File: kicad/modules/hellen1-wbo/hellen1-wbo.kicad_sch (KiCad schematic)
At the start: 58 parts, among them J600 Conn_02x03_Odd_Even, M600 Module-wbo-0.2, Q600 BTS3028, U600 MCP6004, U601 AD8628, U602 STM32F042K6Tx, U603 REF3033, U604 XC6206P332MR

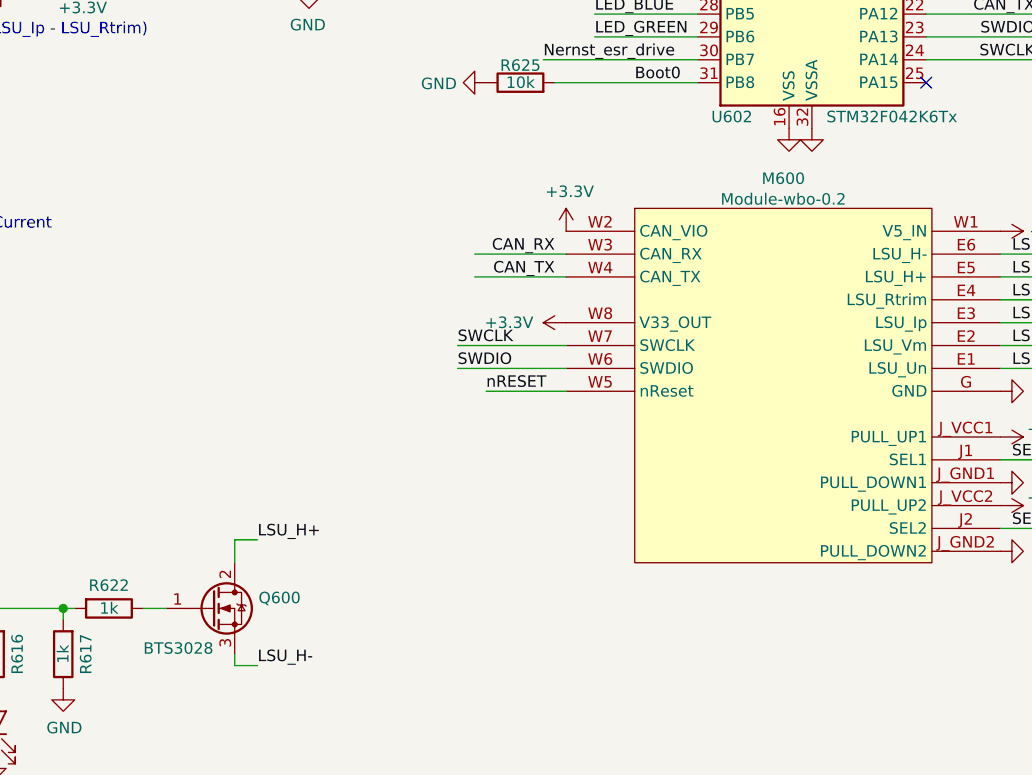
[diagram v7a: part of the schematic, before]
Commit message: wbo-0.3 https://github.com/andreika-git/hellen-one/issues/96
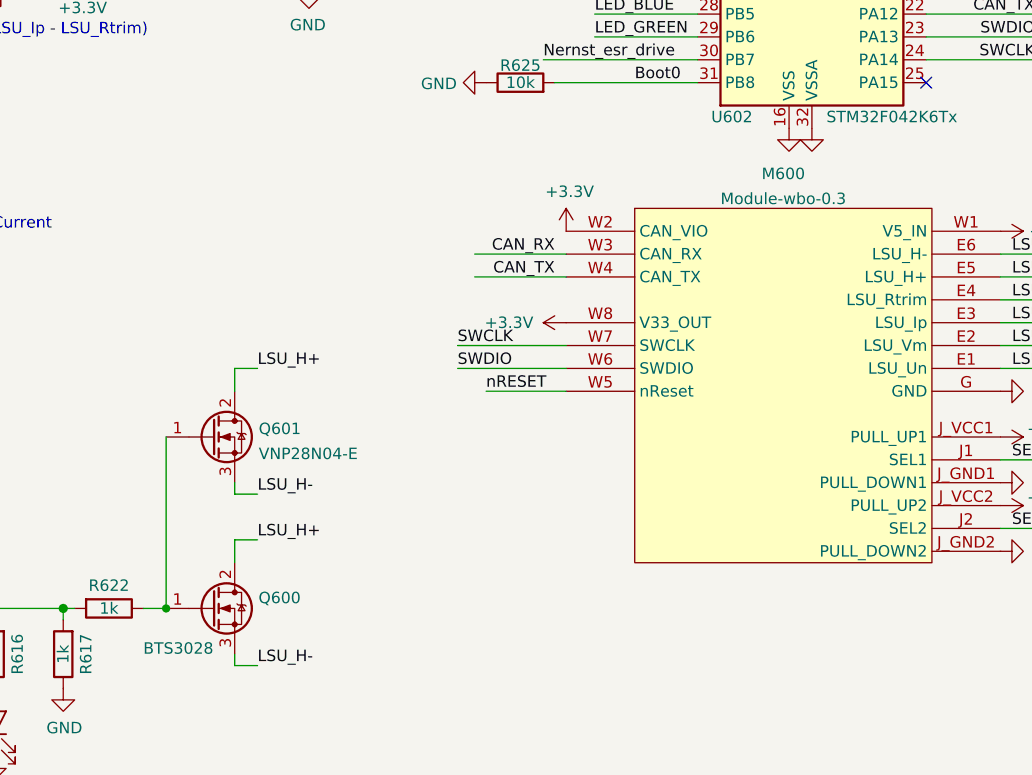
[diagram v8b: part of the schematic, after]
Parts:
- removed M600: Module-wbo-0.2, hellen-one-wbo-0.2:wbo, symbol hellen-one-wbo-0.2:Module-wbo-0.2
- added M600: Module-wbo-0.3, hellen-one-wbo-0.3:wbo, symbol hellen-one-wbo-0.3:Module-wbo-0.3
- added Q601: VNP28N04-E, Package_TO_SOT_THT:TO-220-3_Vertical, symbol Transistor_FET:VNP10N07
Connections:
- net +3V3: now also M600.J_VCC1 (PULL_UP1), M600.J_VCC2 (PULL_UP2), M600.W2 (CAN_VIO), M600.W8 (V33_OUT)
- net +5V: now also M600.W1 (V5_IN)
- net CAN_RX: now also M600.W3 (CAN_RX)
- net CAN_TX: now also M600.W4 (CAN_TX)
- net GND: now also M600.G (GND), M600.J_GND1 (PULL_DOWN1), M600.J_GND2 (PULL_DOWN2)
- net LSU_H+: now also M600.E5 (LSU_H+), Q601.2 (D)
- net LSU_H-: now also M600.E6 (LSU_H-), Q601.3 (S)
- net LSU_Ip: now also M600.E3 (LSU_Ip)
- net LSU_Rtrim: now also M600.E4 (LSU_Rtrim)
- net LSU_Un: now also M600.E1 (LSU_Un)
- net LSU_Vm: now also M600.E2 (LSU_Vm)
- net SEL1: now also M600.J1 (SEL1)
- net SEL2: now also M600.J2 (SEL2)
- net SWCLK: now also M600.W7 (SWCLK)
- net SWDIO: now also M600.W6 (SWDIO)
- net nRESET: now also M600.W5 (nReset)
- net at Q600.1 (G), R622.1: now also Q601.1 (G)
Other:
- company: (none) -> rusefi.com
- title: (none) -> WBO
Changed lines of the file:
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@@
-(kicad_sch (version 20210406) (generator eeschema)
+(kicad_sch (version 20210621) (generator eeschema)
   (paper "A4")
+  (title_block
+    (title "WBO")
+    (date "2021-09-28")
+    (rev "0.3")
+    (company "rusefi.com")
+  )
   (junction (at 27.94 32.385) (diameter 1.016) (color 0 0 0 0))
   (junction (at 39.37 142.24) (diameter 1.016) (color 0 0 0 0))
@@
   (junction (at 115.57 27.94) (diameter 1.016) (color 0 0 0 0))
   (junction (at 115.57 33.02) (diameter 1.016) (color 0 0 0 0))
+  (junction (at 116.84 166.37) (diameter 0) (color 0 0 0 0))
   (junction (at 120.65 87.63) (diameter 1.016) (color 0 0 0 0))
   (junction (at 135.89 30.48) (diameter 1.016) (color 0 0 0 0))
@@
     (stroke (width 0) (type solid) (color 0 0 0 0))
   )
+  (wire (pts (xy 116.84 147.32) (xy 116.84 166.37))
+    (stroke (width 0) (type default) (color 0 0 0 0))
+  )
   (wire (pts (xy 116.84 166.37) (xy 114.3 166.37))
     (stroke (width 0) (type solid) (color 0 0 0 0))
@@
   )
   (wire (pts (xy 120.65 87.63) (xy 123.19 87.63))
+    (stroke (width 0) (type solid) (color 0 0 0 0))
+  )
+  (wire (pts (xy 124.46 139.7) (xy 127 139.7))
+    (stroke (width 0) (type solid) (color 0 0 0 0))
+  )
+  (wire (pts (xy 124.46 142.24) (xy 124.46 139.7))
+    (stroke (width 0) (type solid) (color 0 0 0 0))
+  )
+  (wire (pts (xy 124.46 152.4) (xy 124.46 153.67))
+    (stroke (width 0) (type solid) (color 0 0 0 0))
+  )
+  (wire (pts (xy 124.46 153.67) (xy 127 153.67))
     (stroke (width 0) (type solid) (color 0 0 0 0))
   )
@@
     (effects (font (size 1.27 1.27)) (justify right bottom))
   )
+  (label "LSU_H+" (at 127 139.7 0)
+    (effects (font (size 1.27 1.27)) (justify left bottom))
+  )
+  (label "LSU_H-" (at 127 153.67 0)
+    (effects (font (size 1.27 1.27)) (justify left bottom))
+  )
   (label "LSU_H+" (at 127 158.75 0)
     (effects (font (size 1.27 1.27)) (justify left bottom))
@@
   (symbol (lib_id "hellen1-wbo-rescue:+3.3V-power") (at 161.29 124.46 0) (unit 1)
     (in_bom yes) (on_board yes)
-    (property "Reference" "#PWR?" (id 0) (at 161.29 128.27 0)
+    (property "Reference" "#PWR01" (id 0) (at 161.29 128.27 0)
       (effects (font (size 1.27 1.27)) hide)
     )
@@
   (symbol (lib_id "hellen1-wbo-rescue:+3.3V-power") (at 161.29 134.62 90) (mirror x) (unit 1)
     (in_bom yes) (on_board yes)
-    (property "Reference" "#PWR?" (id 0) (at 165.1 134.62 0)
+    (property "Reference" "#PWR02" (id 0) (at 165.1 134.62 0)
       (effects (font (size 1.27 1.27)) hide)
     )
@@
   (symbol (lib_id "hellen1-wbo-rescue:+3.3V-power") (at 209.55 147.32 270) (unit 1)
     (in_bom yes) (on_board yes)
-    (property "Reference" "#PWR?" (id 0) (at 205.74 147.32 0)
+    (property "Reference" "#PWR03" (id 0) (at 205.74 147.32 0)
       (effects (font (size 1.27 1.27)) hide)
     )
@@
   (symbol (lib_id "hellen1-wbo-rescue:+3.3V-power") (at 209.55 154.94 270) (unit 1)
     (in_bom yes) (on_board yes)
-    (property "Reference" "#PWR?" (id 0) (at 205.74 154.94 0)
+    (property "Reference" "#PWR05" (id 0) (at 205.74 154.94 0)
       (effects (font (size 1.27 1.27)) hide)
     )
@@
   (symbol (lib_id "hellen1-wbo-rescue:GND-power") (at 209.55 152.4 90) (unit 1)
     (in_bom yes) (on_board yes)
-    (property "Reference" "#PWR?" (id 0) (at 215.9 152.4 0)
+    (property "Reference" "#PWR04" (id 0) (at 215.9 152.4 0)
       (effects (font (size 1.27 1.27)) hide)
     )
@@
   (symbol (lib_id "hellen1-wbo-rescue:GND-power") (at 209.55 160.02 90) (unit 1)
     (in_bom yes) (on_board yes)
-    (property "Reference" "#PWR?" (id 0) (at 215.9 160.02 0)
+    (property "Reference" "#PWR06" (id 0) (at 215.9 160.02 0)
       (effects (font (size 1.27 1.27)) hide)
     )
@@
     (pin "1")
     (pin "2")
+  )
+  (symbol (lib_id "Transistor_FET:VNP10N07") (at 121.92 147.32 0) (unit 1)
+    (in_bom yes) (on_board yes) (fields_autoplaced)
+    (property "Reference" "Q601" (id 0) (at 127.1271 146.4115 0)
+      (effects (font (size 1.27 1.27)) (justify left))
+    )
+    (property "Value" "VNP28N04-E" (id 1) (at 127.1271 149.1866 0)
+      (effects (font (size 1.27 1.27)) (justify left))
+    )
+    (property "Footprint" "Package_TO_SOT_THT:TO-220-3_Vertical" (id 2) (at 128.27 149.225 0)
+      (effects (font (size 1.27 1.27) italic) (justify left) hide)
+    )
+    (property "Datasheet" "" (id 3) (at 121.92 147.32 0)
+      (effects (font (size 1.27 1.27)) (justify left) hide)
+    )
+    (property "LCSC" "C263002" (id 4) (at 121.92 147.32 0)
+      (effects (font (size 1.27 1.27)) hide)
+    )
+    (pin "1")
+    (pin "2")
+    (pin "3")
+  )
+  (symbol (lib_id "hellen1-wbo-rescue:Q_NMOS_GDS-Device") (at 121.92 166.37 0) (unit 1)
+    (in_bom yes) (on_board yes)
+    (property "Reference" "Q600" (id 0) (at 127.1016 165.2016 0)
+      (effects (font (size 1.27 1.27)) (justify left))
+    )
+    (property "Value" "BTS3028" (id 1) (at 114.3 170.815 0)
+      (effects (font (size 1.27 1.27)) (justify left))
+    )
+    (property "Footprint" "Package_TO_SOT_SMD:TO-252-2" (id 2) (at 127 163.83 0)
+      (effects (font (size 1.27 1.27)) hide)
+    )
+    (property "Datasheet" "~" (id 3) (at 121.92 166.37 0)
+      (effects (font (size 1.27 1.27)) hide)
+    )
+    (property "LCSC" "C112639" (id 4) (at 121.92 166.37 0)
+      (effects (font (size 1.27 1.27)) hide)
+    )
+    (pin "1")
+    (pin "2")
+    (pin "3")
   )
   (symbol (lib_id "Connector_Generic:Conn_02x03_Odd_Even") (at 254 33.02 0) (unit 1)
@@
     (pin "5")
     (pin "6")
-  )
-  (symbol (lib_id "hellen1-wbo-rescue:Q_NMOS_GDS-Device") (at 121.92 166.37 0) (unit 1)
-    (in_bom yes) (on_board yes)
-    (property "Reference" "Q600" (id 0) (at 127.1016 165.2016 0)
-      (effects (font (size 1.27 1.27)) (justify left))
-    )
-    (property "Value" "BTS3028" (id 1) (at 114.3 170.815 0)
-      (effects (font (size 1.27 1.27)) (justify left))
-    )
-    (property "Footprint" "Package_TO_SOT_SMD:TO-252-2" (id 2) (at 127 163.83 0)
-      (effects (font (size 1.27 1.27)) hide)
-    )
-    (property "Datasheet" "~" (id 3) (at 121.92 166.37 0)
-      (effects (font (size 1.27 1.27)) hide)
-    )
-    (property "LCSC" "C112639" (id 4) (at 121.92 166.37 0)
-      (effects (font (size 1.27 1.27)) hide)
-    )
-    (pin "1")
-    (pin "2")
-    (pin "3")
   )
   (symbol (lib_id "hellen1-wbo-rescue:XC6206PxxxMR-Regulator_Linear") (at 250.825 139.065 0) (unit 1)
@@
     (pin "9")
   )
-  (symbol (lib_id "hellen-one-wbo-0.2:Module-wbo-0.2") (at 168.91 121.92 0) (unit 1)
+  (symbol (lib_id "hellen-one-wbo-0.3:Module-wbo-0.3") (at 168.91 121.92 0) (unit 1)
     (in_bom yes) (on_board yes) (fields_autoplaced)
-    (property "Reference" "M600" (id 0) (at 185.42 118.6138 0))
-    (property "Value" "Module-wbo-0.2" (id 1) (at 185.42 120.9125 0))
-    (property "Footprint" "hellen-one-wbo-0.2:wbo" (id 2) (at 194.31 120.65 0)
+    (property "Reference" "M600" (id 0) (at 185.42 118.0804 0))
+    (property "Value" "Module-wbo-0.3" (id 1) (at 185.42 120.8555 0))
+    (property "Footprint" "hellen-one-wbo-0.3:wbo" (id 2) (at 194.31 120.65 0)
       (effects (font (size 1.27 1.27)) hide)
     )
@@
       (reference "#FLG0601") (unit 1) (value "PWR_FLAG") (footprint "")
     )
+    (path "/85464752-66ec-4a65-8d45-ea14c184e4d2"
+      (reference "#PWR01") (unit 1) (value "+3.3V") (footprint "")
+    )
+    (path "/6ac4b304-1d58-401a-a4a8-775f6dbed43e"
+      (reference "#PWR02") (unit 1) (value "+3.3V") (footprint "")
+    )
+    (path "/ff6c7081-9e18-4197-bee7-9f242433e34c"
+      (reference "#PWR03") (unit 1) (value "+3.3V") (footprint "")
+    )
+    (path "/60473116-363f-4ad0-a211-e8668ba00e3f"
+      (reference "#PWR04") (unit 1) (value "GND") (footprint "")
+    )
+    (path "/f3278198-5958-4dd8-bc33-4373cfed78c1"
+      (reference "#PWR05") (unit 1) (value "+3.3V") (footprint "")
+    )
+    (path "/b74a179f-999b-42b0-958b-4fe7f057860c"
+      (reference "#PWR06") (unit 1) (value "GND") (footprint "")
+    )
     (path "/00000000-0000-0000-0000-00005eb130b2"
       (reference "#PWR0600") (unit 1) (value "GND") (footprint "")
@@
       (reference "#PWR0649") (unit 1) (value "GND") (footprint "")
     )
-    (path "/60473116-363f-4ad0-a211-e8668ba00e3f"
-      (reference "#PWR?") (unit 1) (value "GND") (footprint "")
-    )
-    (path "/6ac4b304-1d58-401a-a4a8-775f6dbed43e"
-      (reference "#PWR?") (unit 1) (value "+3.3V") (footprint "")
-    )
-    (path "/85464752-66ec-4a65-8d45-ea14c184e4d2"
-      (reference "#PWR?") (unit 1) (value "+3.3V") (footprint "")
-    )
-    (path "/b74a179f-999b-42b0-958b-4fe7f057860c"
-      (reference "#PWR?") (unit 1) (value "GND") (footprint "")
-    )
-    (path "/f3278198-5958-4dd8-bc33-4373cfed78c1"
-      (reference "#PWR?") (unit 1) (value "+3.3V") (footprint "")
-    )
-    (path "/ff6c7081-9e18-4197-bee7-9f242433e34c"
-      (reference "#PWR?") (unit 1) (value "+3.3V") (footprint "")
-    )
     (path "/00000000-0000-0000-0000-00005eb1294f"
       (reference "C600") (unit 1) (value "1u") (footprint "Capacitor_SMD:C_0402_1005Metric")
@@
       (reference "J600") (unit 1) (value "Conn_02x03_Odd_Even") (footprint "Connector:Tag-Connect_TC2030-IDC-NL_2x03_P1.27mm_Vertical")
     )
-    (path "/82294612-ed07-4aec-a8a4-b27becb52ff6"
-      (reference "M600") (unit 1) (value "Module-wbo-0.2") (footprint "hellen-one-wbo-0.2:wbo")
+    (path "/b31bd6a2-d597-4ef3-ad7d-f0d5e79bcc1c"
+      (reference "M600") (unit 1) (value "Module-wbo-0.3") (footprint "hellen-one-wbo-0.3:wbo")
     )
     (path "/00000000-0000-0000-0000-0000600e1a2d"
       (reference "Q600") (unit 1) (value "BTS3028") (footprint "Package_TO_SOT_SMD:TO-252-2")
     )
+    (path "/57e3250d-e0a0-4878-88b9-8522d970b2ae"
+      (reference "Q601") (unit 1) (value "VNP28N04-E") (footprint "Package_TO_SOT_THT:TO-220-3_Vertical")
+    )
     (path "/00000000-0000-0000-0000-00005eb0f879"
